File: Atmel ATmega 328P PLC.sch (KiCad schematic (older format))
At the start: 4 parts

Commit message: Added all schematic components, annotated and asigned!
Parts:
- added C1, C2, C3, C4, C5, C6: C, Capacitor_SMD:C_0603_1608Metric_Pad1.05x0.95mm_HandSolder, symbol Device:C
- added D3, D4: LED, LED_SMD:LED_0603_1608Metric_Pad1.05x0.95mm_HandSolder, symbol Device:LED
- added J1: Conn_01x06_Male, Connector_PinHeader_2.54mm:PinHeader_1x06_P2.54mm_Vertical, symbol Connector:Conn_01x06_Male
- added J2: Conn_01x04_Male, Connector_PinHeader_2.54mm:PinHeader_1x04_P2.54mm_Vertical, symbol Connector:Conn_01x04_Male
- added J3: Conn_02x03_Odd_Even, Connector_PinHeader_1.27mm:PinHeader_2x03_P1.27mm_Vertical, symbol Connector_Generic:Conn_02x03_Odd_Even
- added R2, R3, R4: R, Resistor_SMD:R_0603_1608Metric_Pad1.05x0.95mm_HandSolder, symbol Device:R
- added SW1: SW_DIP_x02, freetronics_footprints:SW_PUSHBUTTON_SMD, symbol Switch:SW_DIP_x02
- added U1: ATmega328P-AU, Package_QFP:TQFP-32_7x7mm_P0.8mm, symbol MCU_Microchip_ATmega:ATmega328P-AU
- added U2: MC7805BDTRKG, digikey-footprints:TO-252-3, symbol dk_PMIC-Voltage-Regulators-Linear:MC7805BDTRKG
- added Y1: Crystal, Crystal:Crystal_SMD_EuroQuartz_MT-4Pin_3.2x2.5mm_HandSoldering, symbol Device:Crystal
- D1: renamed from D?; value DIODE -> D; footprint (none) -> Diode_SMD:D_SMA_Handsoldering; symbol freetronics_schematic:DIODE -> Device:D
- D2: renamed from D?; footprint (none) -> LED_SMD:LED_0603_1608Metric_Pad1.05x0.95mm_HandSolder
- J4: renamed from J?; footprint (none) -> TerminalBlock_Phoenix:TerminalBlock_Phoenix_PT-1,5-2-5.0-H_1x02_P5.00mm_Horizontal
- R1: renamed from R?; footprint (none) -> Resistor_SMD:R_0603_1608Metric_Pad1.05x0.95mm_HandSolder
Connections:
- new net: U1.21 (GND), U1.3 (GND), U1.5 (GND)
- new net: U1.4 (VCC), U1.6 (VCC)
- new net DTR: J1.1 (Pin_1)
- new net MISO: J3.1 (Pin_1)
- new net MOSI: J3.4 (Pin_4), U1.16 (PB4)
- new net PB0: U1.12 (PB0)
- new net PB1: U1.13 (PB1)
- new net PB2: U1.14 (PB2)
- new net PC0: U1.23 (PC0)
- new net PC1: U1.24 (PC1)
- new net PD2: U1.32 (PD2)
- new net PD3: U1.1 (PD3)
- new net PD4: U1.2 (PD4)
- new net PD5: U1.9 (PD5)
- new net PD6: U1.10 (PD6)
- new net PD7: U1.11 (PD7)
- new net RESET: J3.5 (Pin_5)
- new net RX: J1.3 (Pin_3), U1.30 (PD0)
- new net SCK: J3.3 (Pin_3)
- new net SCL: J2.3 (Pin_3), U1.28 (PC5)
- new net SDA: J2.2 (Pin_2), U1.27 (PC4)
- new net TX: J1.2 (Pin_2), U1.31 (PD1)
- no-connect marks 0 -> 4
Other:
- moved on the sheet: D1, D2, J4, R1

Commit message: Finished schematic with all elements.
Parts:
- removed SW1: SW_DIP_x02, freetronics_footprints:SW_PUSHBUTTON_SMD, symbol Switch:SW_DIP_x02
- added SW1: SW_DIP_x02, freetronics_footprints:SW_PUSHBUTTON_SMD, symbol Switch_JLCPCB:SW_DIP_x02
- C1: value C -> 1uF 10V
- C2: renamed from C5; value C -> 22pF 10V
- C3: renamed from C6; value C -> 22pF 10V
- C4: renamed from C2; value C -> 10uF 35V; footprint Capacitor_SMD:C_0603_1608Metric_Pad1.05x0.95mm_HandSolder -> Capacitor_SMD:C_Elec_4x5.8; symbol Device:C -> Device:CP
- C5: renamed from C4; value C -> 0.1uF 10V
- C6: renamed from C3; value C -> 10uF 35V; footprint Capacitor_SMD:C_0603_1608Metric_Pad1.05x0.95mm_HandSolder -> Capacitor_SMD:C_Elec_4x5.8; symbol Device:C -> Device:CP
- D1: value D -> 1A
- D2: value LED -> RED
- D3: renamed from D4; value LED -> GREEN
- D4: renamed from D3; value LED -> RED
- R1: value R -> 2k2
- R2: renamed from R3; value R -> 10k
- R3: renamed from R4; value R -> 220R
- R4: renamed from R2; value R -> 220R
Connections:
- net +24V: now also C4.1, D1.1 (K), R1.1, U2.1 (IN)
- net +5V: now also C6.1, J1.4 (Pin_4), J2.1 (Pin_1), J3.2 (Pin_2), R2.1, R4.1, U1.18 (AVCC), U1.4 (VCC), U1.6 (VCC), U2.3 (OUT)
- net DTR: now also C5.1
- net GND: now also C1.2, C2.1, C3.1, C4.2, C6.2, D2.1 (K), D3.1 (K), D4.1 (K), J1.5 (Pin_5), J1.6 (Pin_6), J2.4 (Pin_4), J3.6 (Pin_6), J4.1 (Pin_1), U1.21 (GND), U1.3 (GND), U1.5 (GND), U2.4 (GND), SW1.2
- net MISO: now also U1.15 (PB3)
- net RESET: now also U1.29 (~RESET~/PC6), SW1.1
- net SCK: now also R3.1, U1.17 (PB5)
- net at J4.2 (Pin_2): now also D1.2 (A)
- net at R1.2: now also D2.2 (A)
- net at R4.2: now also D4.2 (A)
- net at U1.20 (AREF): now also C1.1
- net at U1.7 (XTAL1/PB6): now also C2.2, Y1.1
- net at U1.8 (XTAL2/PB7): now also C3.2, Y1.2
- net at R3.2: now also D3.2 (A)
- net at C5.2: now also R2.2, SW1.1
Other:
- note added: "24V to 5V"
- note added: "ATmega 328P-AU"
- note added: "I2C"
- note added: "ICSP"
- note added: "UART"
- moved on the sheet: C1, C2, C3, C5, D1, D2, D3, D4, J1, J2, J3, J4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

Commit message: Share with FB KiCad group!
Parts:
- J3: footprint Connector_PinHeader_1.27mm:PinHeader_2x03_P1.27mm_Vertical -> Connector_PinHeader_2.54mm:PinHeader_2x03_P2.54mm_Vertical
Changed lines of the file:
@@
 Sheet 1 3
 Title "Atmel ATmega 328P PLC"
-Date "2019-11-21"
+Date "2019-12-11"
 Rev "v.1.0"
 Comp ""
@@
 F 0 "J3" H 1500 5117 50  0000 C CNN
 F 1 "Conn_02x03_Odd_Even" H 1500 5026 50  0000 C CNN
-F 2 "Connector_PinHeader_1.27mm:PinHeader_2x03_P1.27mm_Vertical" H 1450 4800 50  0001 C CNN
+F 2 "Connector_PinHeader_2.54mm:PinHeader_2x03_P2.54mm_Vertical" H 1450 4800 50  0001 C CNN
 F 3 "~" H 1450 4800 50  0001 C CNN
 	1    1450 4800

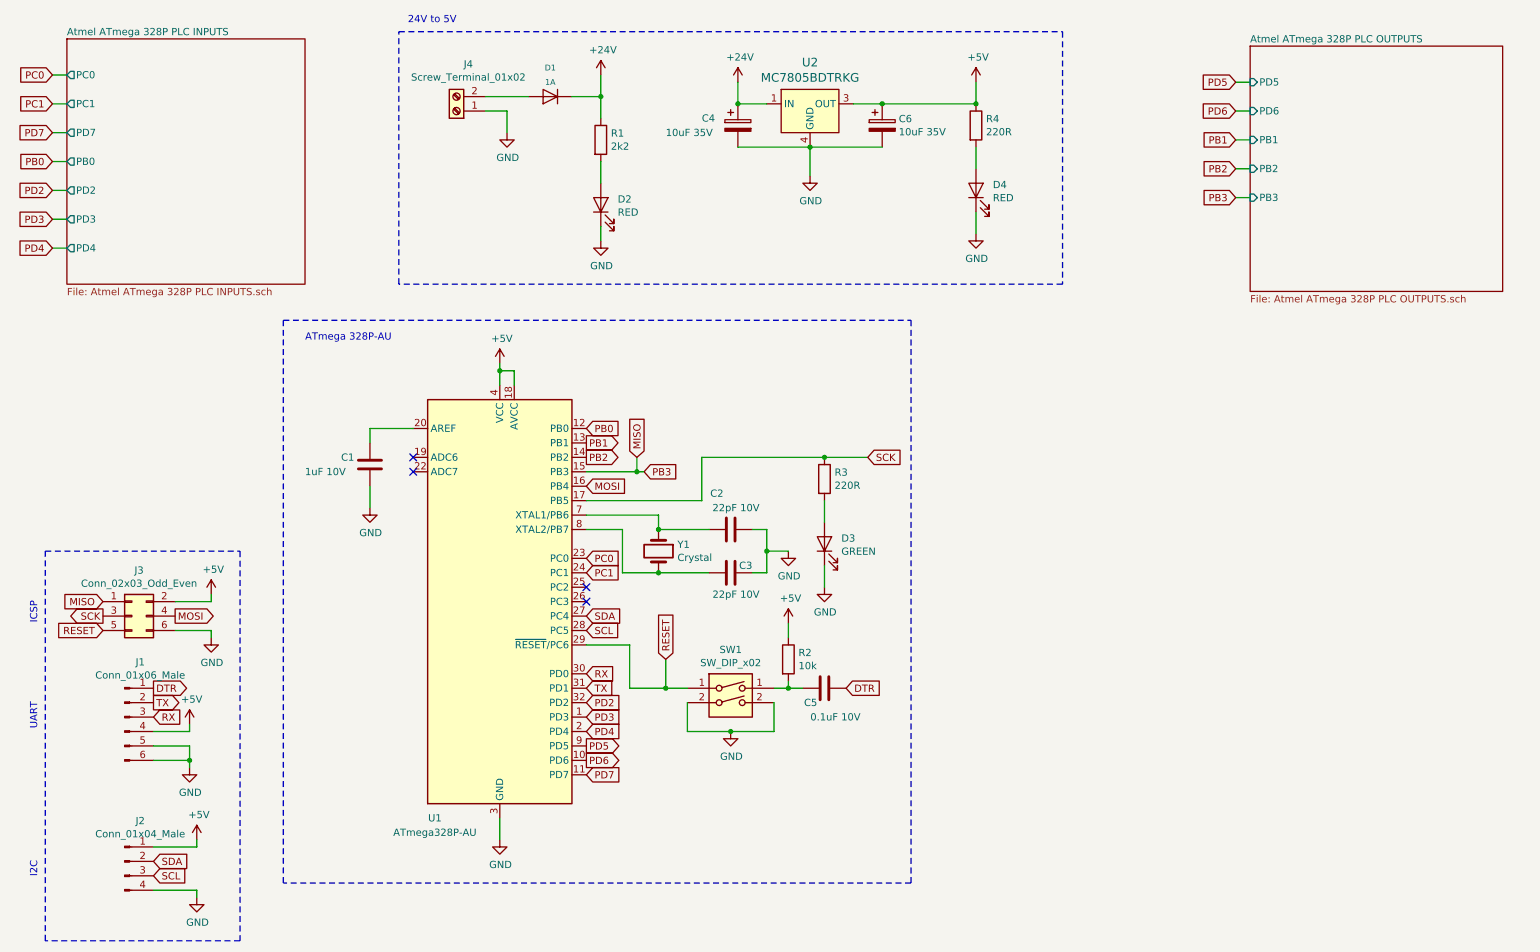
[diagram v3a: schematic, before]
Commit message: Drawed new 24V to 5V 3A switching power supply!
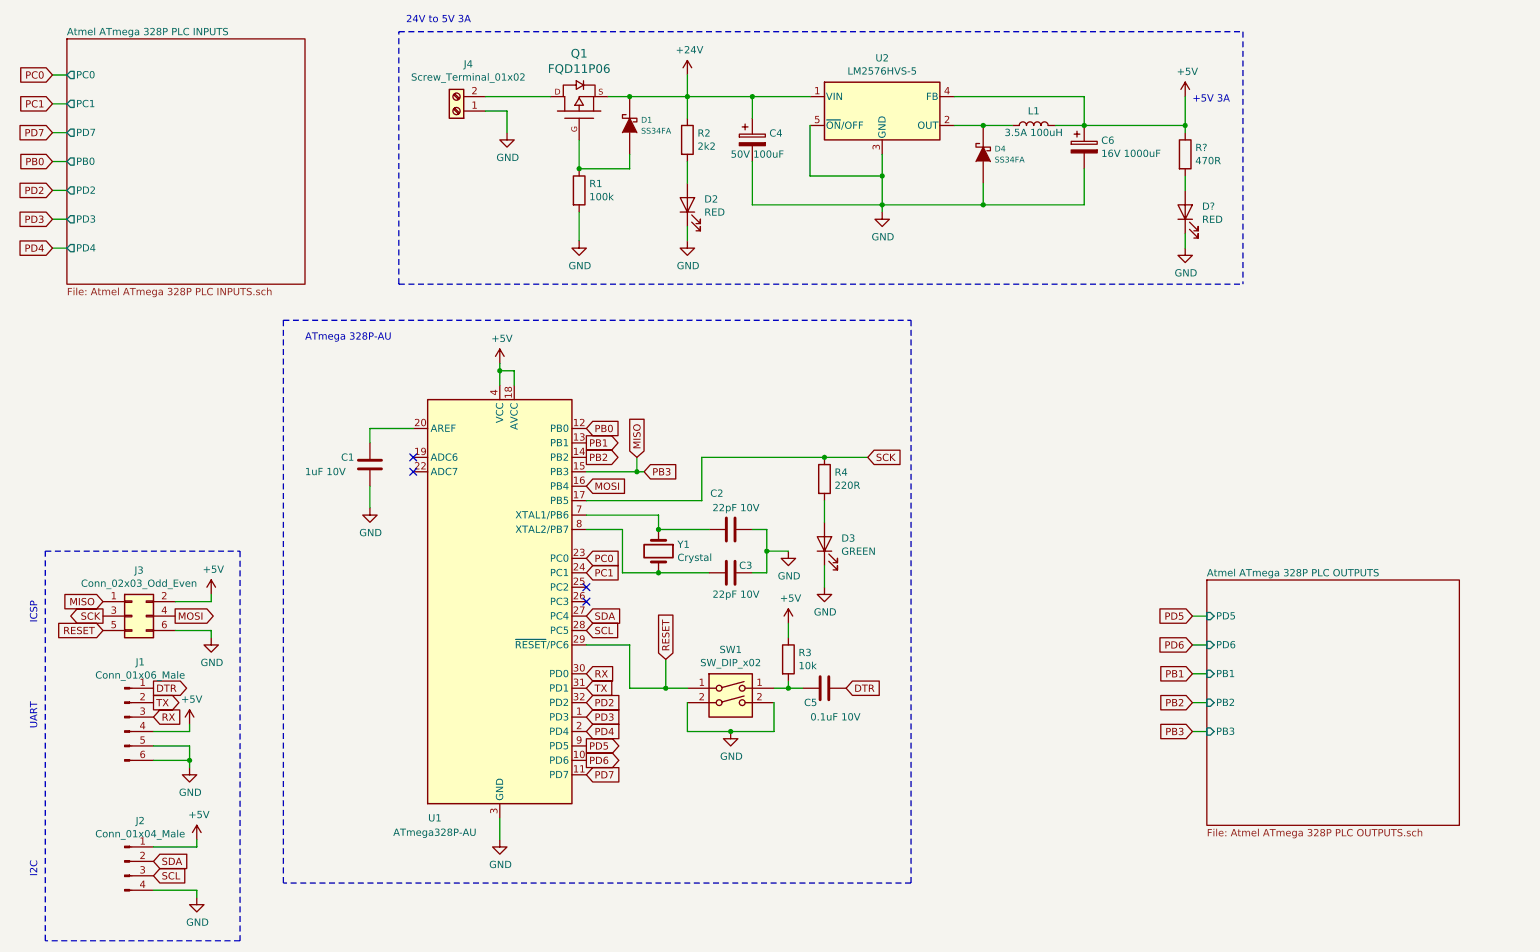
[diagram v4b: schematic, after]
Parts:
- removed D1: 1A, Diode_SMD:D_SMA_Handsoldering, symbol Device:D
- removed D4: RED, LED_SMD:LED_0603_1608Metric_Pad1.05x0.95mm_HandSolder, symbol Device:LED
- removed R4: 220R, Resistor_SMD:R_0603_1608Metric_Pad1.05x0.95mm_HandSolder, symbol Device:R
- removed U2: MC7805BDTRKG, digikey-footprints:TO-252-3, symbol dk_PMIC-Voltage-Regulators-Linear:MC7805BDTRKG
- added D1, D4: SS34FA, Diode_SMD:D_SMA, symbol freetronics_schematic:DIODE_SCHOTTKY
- added D?: RED, LED_SMD:LED_0603_1608Metric_Pad1.05x0.95mm_HandSolder, symbol Device:LED
- added L1: 3.5A 100uH, symbol Device:L
- added Q1: FQD11P06, digikey-footprints:TO-252-3, symbol freetronics_schematic:MOSFET_P
- added R1: 100k, Resistor_SMD:R_0805_2012Metric_Pad1.15x1.40mm_HandSolder, symbol Device:R
- added R?: 470R, Resistor_SMD:R_0603_1608Metric_Pad1.05x0.95mm_HandSolder, symbol Device:R
- added U2: LM2576HVS-5, Package_TO_SOT_SMD:TO-263-5_TabPin3, symbol Regulator_Switching:LM2576HVS-5
- C4: value 10uF 35V -> 50V 100uF; footprint Capacitor_SMD:C_Elec_4x5.8 -> Capacitor_SMD:CP_Elec_8x10
- C6: value 10uF 35V -> 16V 1000uF; footprint Capacitor_SMD:C_Elec_4x5.8 -> Capacitor_SMD:CP_Elec_10x10
- renumbered R1 to R2, R2 to R3, R3 to R4
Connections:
- net +24V: now also D1.K, Q1.S, U2.1 (VIN)
- net +5V: now also L1.2, R?.1, U2.4 (FB)
- net GND: now also D4.A, D?.1 (K), R1.2, U2.3 (GND), U2.5 (~ON~/OFF)
- net at J4.2 (Pin_2): now also Q1.D
- new net: D1.A, Q1.G, R1.1
- new net: D4.K, L1.1, U2.2 (OUT)
- new net: D?.2 (A), R?.2
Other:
- note added: "+5V 3A"
- note added: "24V to 5V 3A"
- note removed: "24V to 5V"
- moved on the sheet: D2, R2
